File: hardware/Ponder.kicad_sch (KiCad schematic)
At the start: 119 parts, among them J1 USB_C_Receptacle_USB2.0, J10 1.27 HDR, J11 2.54 SKT, J12 2.54 SKT, J2 2.54 HDR, J3 2.54 HDR, J4 2.54 HDR, J5 2.54 HDR, J6 2.54 HDR, J7 2.54 HDR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

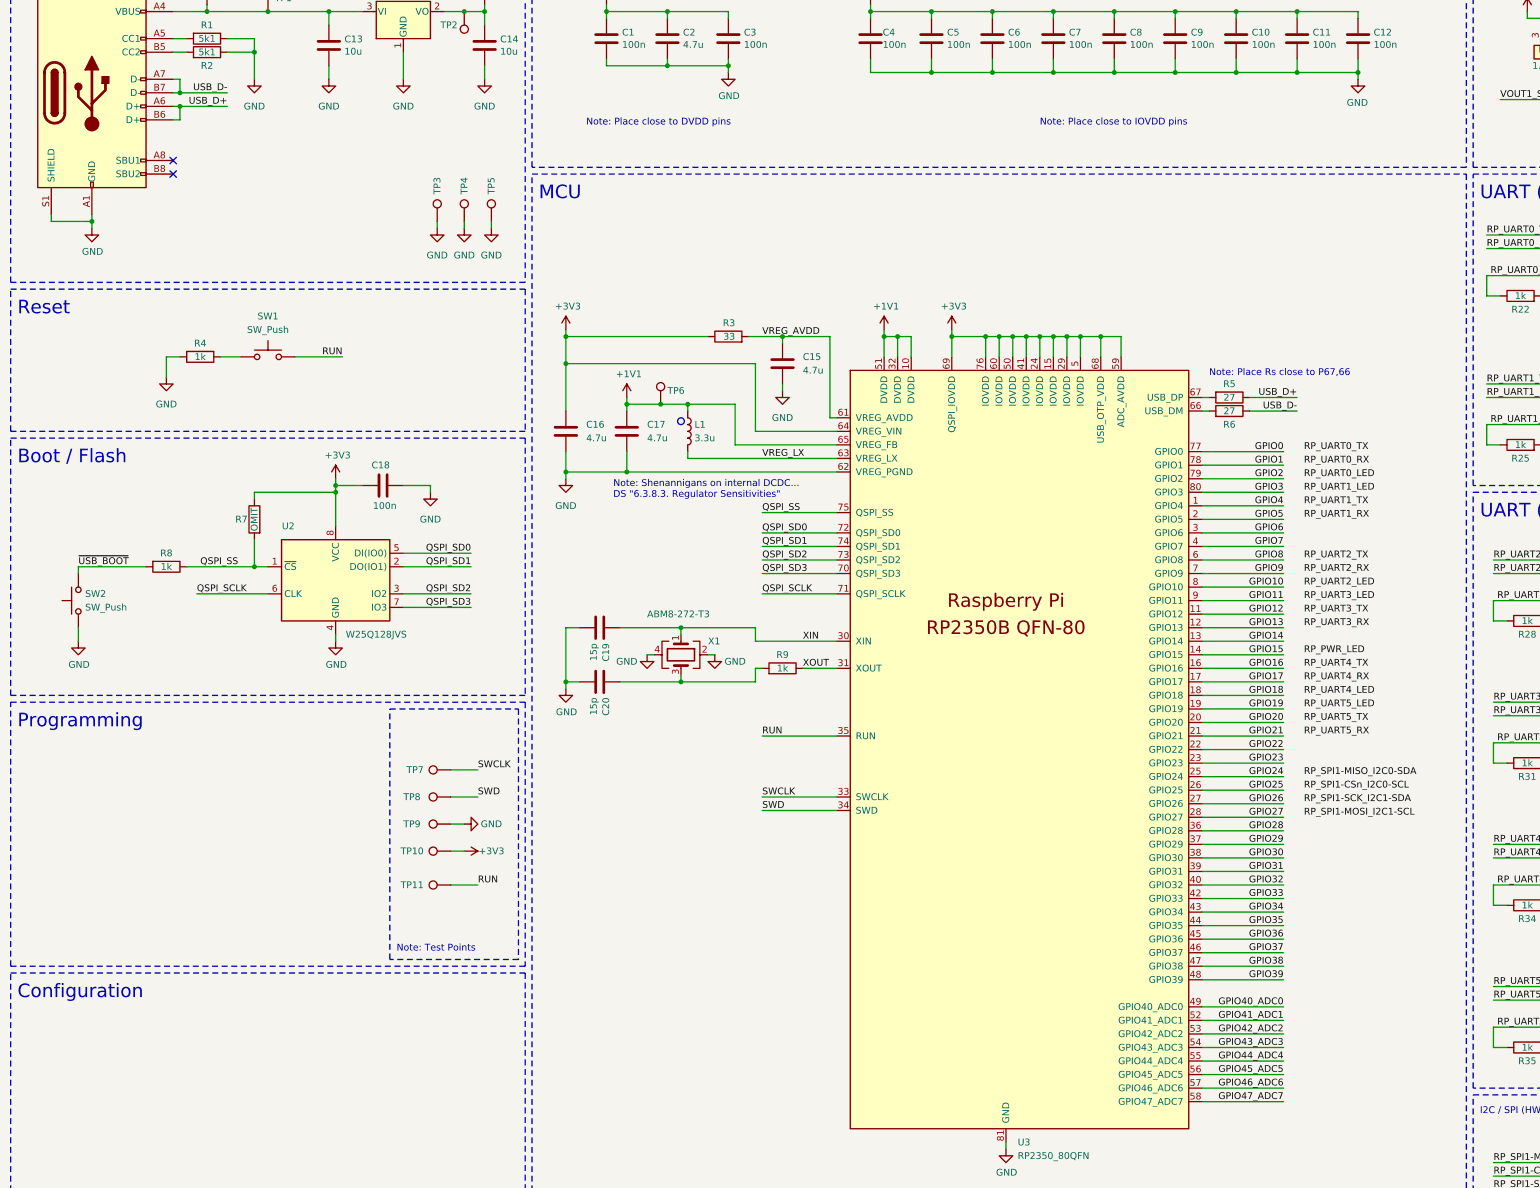
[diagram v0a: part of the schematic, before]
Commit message: Adding LEDs for power status
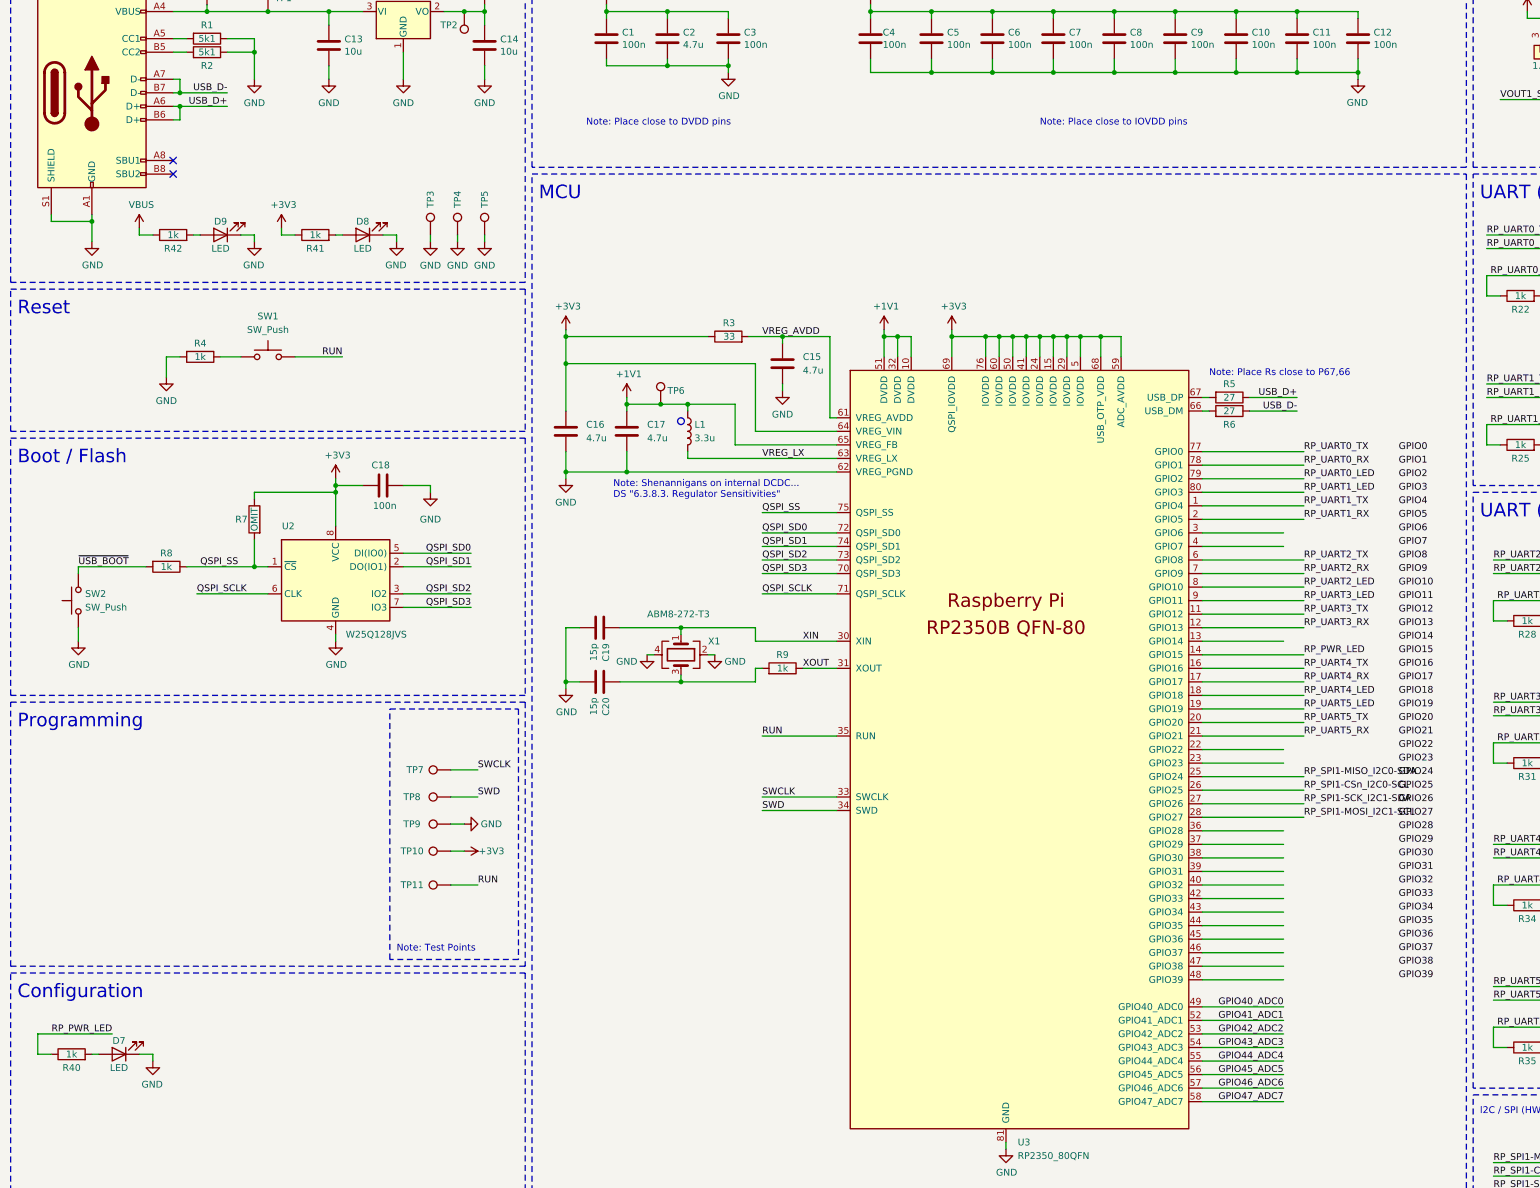
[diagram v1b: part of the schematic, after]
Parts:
- added D7, D8, D9: LED, LED_SMD:LED_0603_1608Metric_Pad1.05x0.95mm_HandSolder, symbol Device:LED
- added R40, R41, R42: 1k, Resistor_SMD:R_0402_1005Metric, symbol Device:R
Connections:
- net +3V3: now also R41.1
- net GND: now also D7.1 (K), D8.1 (K), D9.1 (K)
- net GPIO0: no longer U3.77 (GPIO0)
- net GPIO1: no longer U3.78 (GPIO1)
- net GPIO10: no longer U3.8 (GPIO10)
- net GPIO11: no longer U3.9 (GPIO11)
- net GPIO12: no longer U3.11 (GPIO12)
- net GPIO13: no longer U3.12 (GPIO13)
- net GPIO14: no longer U3.13 (GPIO14)
- net GPIO15: no longer U3.14 (GPIO15)
- net GPIO16: no longer U3.16 (GPIO16)
- net GPIO17: no longer U3.17 (GPIO17)
- net GPIO18: no longer U3.18 (GPIO18)
- net GPIO19: no longer U3.19 (GPIO19)
- net GPIO2: no longer U3.79 (GPIO2)
- net GPIO20: no longer U3.20 (GPIO20)
- net GPIO21: no longer U3.21 (GPIO21)
- net GPIO22: no longer U3.22 (GPIO22)
- net GPIO23: no longer U3.23 (GPIO23)
- net GPIO24: no longer U3.25 (GPIO24)
- net GPIO25: no longer U3.26 (GPIO25)
- net GPIO26: no longer U3.27 (GPIO26)
- net GPIO27: no longer U3.28 (GPIO27)
- net GPIO28: no longer U3.36 (GPIO28)
- net GPIO29: no longer U3.37 (GPIO29)
- net GPIO3: no longer U3.80 (GPIO3)
- net GPIO30: no longer U3.38 (GPIO30)
- net GPIO31: no longer U3.39 (GPIO31)
- net GPIO32: no longer U3.40 (GPIO32)
- net GPIO33: no longer U3.42 (GPIO33)
- net GPIO34: no longer U3.43 (GPIO34)
- net GPIO35: no longer U3.44 (GPIO35)
- net GPIO36: no longer U3.45 (GPIO36)
- net GPIO37: no longer U3.46 (GPIO37)
- net GPIO38: no longer U3.47 (GPIO38)
- net GPIO39: no longer U3.48 (GPIO39)
- net GPIO4: no longer U3.1 (GPIO4)
- net GPIO5: no longer U3.2 (GPIO5)
- net GPIO6: no longer U3.3 (GPIO6)
- net GPIO7: no longer U3.4 (GPIO7)
- net GPIO8: no longer U3.6 (GPIO8)
- net GPIO9: no longer U3.7 (GPIO9)
- net RP_PWR_LED: now also U3.14 (GPIO15), R40.1
- net RP_SPI1-CSn_I2C0-SCL: now also U3.26 (GPIO25)
- net RP_SPI1-MISO_I2C0-SDA: now also U3.25 (GPIO24)
- net RP_SPI1-MOSI_I2C1-SCL: now also U3.28 (GPIO27)
- net RP_SPI1-SCK_I2C1-SDA: now also U3.27 (GPIO26)
- net RP_UART0_LED: now also U3.79 (GPIO2)
- net RP_UART0_RX: now also U3.78 (GPIO1)
- net RP_UART0_TX: now also U3.77 (GPIO0)
- net RP_UART1_LED: now also U3.80 (GPIO3)
- net RP_UART1_RX: now also U3.2 (GPIO5)
- net RP_UART1_TX: now also U3.1 (GPIO4)
- net RP_UART2_LED: now also U3.8 (GPIO10)
- net RP_UART2_RX: now also U3.7 (GPIO9)
- net RP_UART2_TX: now also U3.6 (GPIO8)
- net RP_UART3_LED: now also U3.9 (GPIO11)
- net RP_UART3_RX: now also U3.12 (GPIO13)
- net RP_UART3_TX: now also U3.11 (GPIO12)
- net RP_UART4_LED: now also U3.18 (GPIO18)
- net RP_UART4_RX: now also U3.17 (GPIO17)
- net RP_UART4_TX: now also U3.16 (GPIO16)
- net RP_UART5_LED: now also U3.19 (GPIO19)
- net RP_UART5_RX: now also U3.21 (GPIO21)
- net RP_UART5_TX: now also U3.20 (GPIO20)
- net VBUS: now also R42.1
- new net: D8.2 (A), R41.2
- new net: D7.2 (A), R40.2
- new net: D9.2 (A), R42.2
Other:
- moved on the sheet: TP3, TP4, TP5

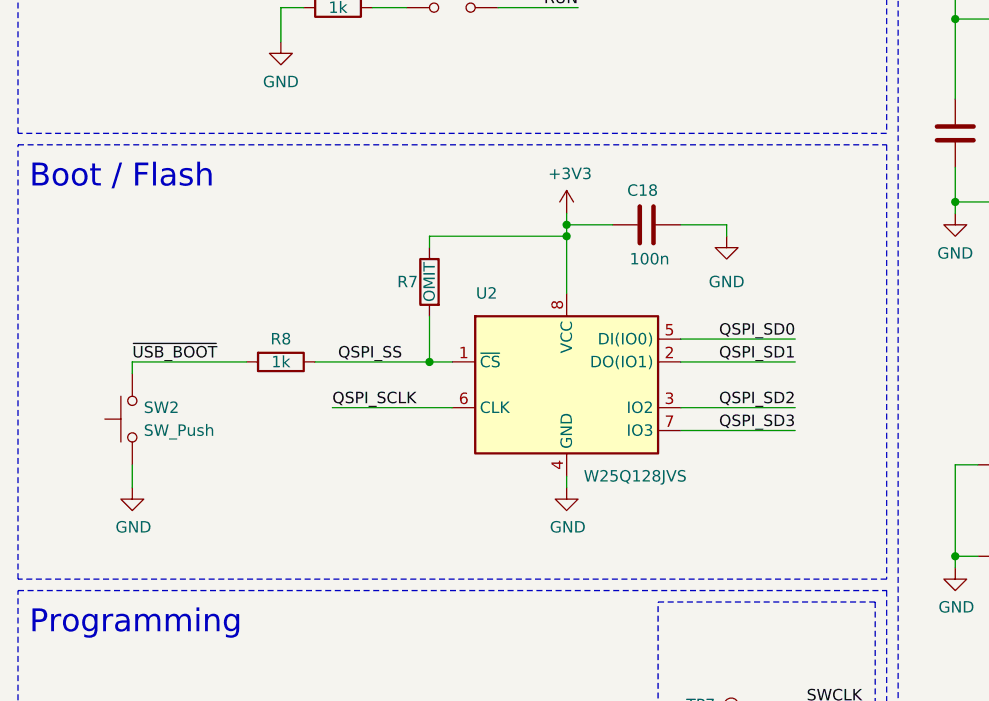
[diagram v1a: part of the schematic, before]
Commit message: Swapping flash in sch for part which isn't the size of a small exoplanet
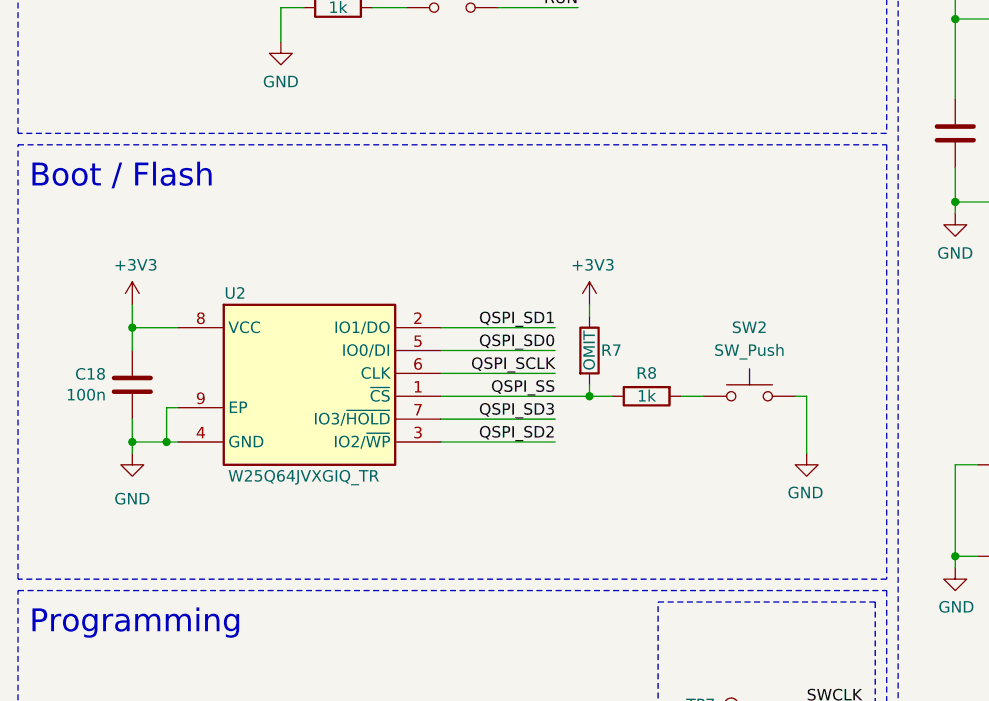
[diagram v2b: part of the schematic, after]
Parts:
- U2: value W25Q128JVS -> W25Q64JVXGIQ_TR; footprint Package_SO:SOIC-8_5.23x5.23mm_P1.27mm -> Ponder:SON80P400X400X50-9N; Height (none) -> 0.5; Manufacturer_Name (none) -> Winbond; Manufacturer_Part_Number (none) -> W25Q64JVXGIQ TR; Mouser Part Number (none) -> 454-W25Q64JVXGIQTR; Mouser Price/Stock (none) -> https://www.mouser.co.uk/ProductDetail/Winbond/W25Q64JVXGIQ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
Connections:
- net GND: now also U2.9 (EP)
- net ~{USB_BOOT}: no longer names the net of R8.2, SW2.2
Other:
- moved on the sheet: R7, R8, SW2

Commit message: First pass layout
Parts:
- removed J10: 1.27 HDR, Connector_PinHeader_1.27mm:PinHeader_1x03_P1.27mm_Horizontal, symbol Connector_Generic:Conn_01x03
- removed J11, J12: 2.54 SKT, Connector_PinSocket_2.54mm:PinSocket_1x02_P2.54mm_Vertical, symbol Connector_Generic:Conn_01x02
- removed TP1, TP2, TP3, TP4, TP5: TestPoint, TestPoint:TestPoint_Pad_D1.0mm, symbol Connector:TestPoint
- added D10: NSR0530HT1G, Diode_SMD:D_SOD-323, symbol Diode:NSR0340HT1G
- added J10: 2.54 SKT, Ponder:M208890245, symbol Connector_Generic:Conn_01x02
- added J11: 2.54 HDR, Connector_PinHeader_2.54mm:PinHeader_1x04_P2.54mm_Vertical_SMD_Pin1Left, symbol Connector_Generic:Conn_01x04
- added R43, R44: 10k, Resistor_SMD:R_0402_1005Metric, symbol Device:R
- added TP10, TP11, TP12, TP7, TP8, TP9: TestPoint, TestPoint:TestPoint_Pad_D1.0mm, symbol Connector:TestPoint
- C16, C17: footprint Capacitor_SMD:C_0402_1005Metric -> Ponder:C_0402_1005Metric_small_pads
- J9: footprint Connector_PinHeader_1.27mm:PinHeader_1x03_P1.27mm_Horizontal -> Connector_PinHeader_1.27mm:PinHeader_1x03_P1.27mm_Vertical
- R7: value OMIT -> 10k
- SW1, SW2: value SW_Push -> 434133025816
- renumbered TP7 to TP1, TP8 to TP2, TP9 to TP3, TP10 to TP4, TP11 to TP5
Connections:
- net GPIO45_ADC5 is gone; now on net RP_UART5_LED: U3.56 (GPIO45_ADC5)
- net GPIO46_ADC6 is gone; now on net RP_UART5_RX: U3.57 (GPIO46_ADC6)
- net GPIO47_ADC7 is gone; now on net RP_UART5_TX: U3.58 (GPIO47_ADC7)
- net VOUT2_SELECT is gone; now on net VOUT1_SELECT: J9.2 (Pin_2)
- net +1V1: no longer TP6.1
- net +3V3: now also R43.1
- net GND: now also SW2.2, J10.1 (Pin_1); no longer SW2.1
- net GPIO15: now also U3.14 (GPIO15), J11.1 (Pin_1)
- net GPIO16: now also U3.16 (GPIO16), J11.2 (Pin_2)
- net GPIO17: now also U3.17 (GPIO17), J11.3 (Pin_3)
- net GPIO18: now also U3.18 (GPIO18), J11.4 (Pin_4)
- net GPIO40_ADC0: now also TP12.1
- net GPIO41_ADC1: now also TP10.1
- net GPIO42_ADC2: now also TP11.1
- net GPIO5: now also TP6.1, U3.2 (GPIO5)
- net GPIO6: now also U3.3 (GPIO6), TP8.1
- net GPIO7: now also U3.4 (GPIO7), TP7.1
- net GPIO9: now also U3.7 (GPIO9), TP9.1
- net QSPI_SS: now also D10.2 (A); no longer R8.1
- net RP_PWR_LED: now also U3.1 (GPIO4); no longer U3.14 (GPIO15)
- net RP_UART1_LED: now also U3.6 (GPIO8); no longer U3.80 (GPIO3)
- net RP_UART1_RX: now also U3.21 (GPIO21); no longer U3.2 (GPIO5)
- net RP_UART1_TX: now also U3.20 (GPIO20); no longer U3.1 (GPIO4)
- net RP_UART2_LED: now also U3.19 (GPIO19); no longer U3.8 (GPIO10)
- net RP_UART2_RX: now also U3.22 (GPIO22); no longer U3.7 (GPIO9)
- net RP_UART2_TX: now also U3.23 (GPIO23); no longer U3.6 (GPIO8)
- net RP_UART3_LED: now also U3.38 (GPIO30); no longer U3.9 (GPIO11)
- net RP_UART3_RX: now also U3.36 (GPIO28); no longer U3.12 (GPIO13)
- net RP_UART3_TX: now also U3.37 (GPIO29); no longer U3.11 (GPIO12)
- net RP_UART4_LED: now also U3.43 (GPIO34); no longer U3.18 (GPIO18)
- net RP_UART4_RX: now also U3.40 (GPIO32); no longer U3.17 (GPIO17)
- net RP_UART4_TX: now also U3.42 (GPIO33); no longer U3.16 (GPIO16)
- net RP_UART5_LED: no longer U3.19 (GPIO19)
- net RP_UART5_RX: no longer U3.21 (GPIO21)
- net RP_UART5_TX: no longer U3.20 (GPIO20)
- net VOUT1_SELECT: now also J10.2 (Pin_2)
- net at R8.2: now also D10.1 (K); no longer SW2.2
- net GPIO43_ADC3: no longer names the net of U3.54 (GPIO43_ADC3)
- net GPIO44_ADC4: no longer names the net of U3.55 (GPIO44_ADC4)
- new net: R43.2, R44.2, R8.1, SW2.1
- new net USR_SW: R44.1, U3.80 (GPIO3)
- no-connect marks 2 -> 15
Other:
- note added: "Flash / Boot & User Switch"
- note added: "Misc"
- note added: "Note: Headers removed - Program via USB"
- note added: "Note: Switch to be used as flash boot inhibit and as user input"
- note added: "Note: User LED, nominally 'power'"
- note added: "Rail Decoupling"
- note added: "Reset Switch"
- note added: "Spare IO"
- note removed: "Boot / Flash"
- note removed: "Configuration"
- note removed: "Rail decoupling"
- note removed: "Reset"
- moved on the sheet: C13, C14, C18, D7, D8, D9, J9, R40, R41, R42, R5, R6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

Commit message: Silk tittivating
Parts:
- added J12, J13, J14, J15: 1.27 HDR, Connector_PinHeader_1.27mm:PinHeader_1x03_P1.27mm_Vertical, symbol Connector_Generic:Conn_01x03
- added R45, R46, R47, R48: 10k, Resistor_SMD:R_0402_1005Metric, symbol Device:R
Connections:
- net +3V3: now also J12.1 (Pin_1), J13.1 (Pin_1), J14.1 (Pin_1), J15.1 (Pin_1)
- net GND: now also J12.3 (Pin_3), J13.3 (Pin_3), J14.3 (Pin_3), J15.3 (Pin_3)
- net RP_SPI1-CSn_I2C0-SCL: now also R48.2
- net RP_SPI1-MISO_I2C0-SDA: now also R47.2
- net RP_SPI1-MOSI_I2C1-SCL: now also R45.2
- net RP_SPI1-SCK_I2C1-SDA: now also R46.2
- new net: J12.2 (Pin_2), R47.1
- new net: J15.2 (Pin_2), R45.1
- new net: J14.2 (Pin_2), R46.1
- new net: J13.2 (Pin_2), R48.1
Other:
- note removed: "TODO - Add selectable pull-ups"
- moved on the sheet: J8
